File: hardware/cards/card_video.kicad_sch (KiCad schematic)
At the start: 48 parts, among them J1 HDMI_A, J2 VGA HD15, M1 Core2350B (8MB PSRAM), U2 74LVC245A, U3 74LVC245A, U4 74LVC245A, U5 74LVC245A, U6 74LVC245A, U7 74LVC245A

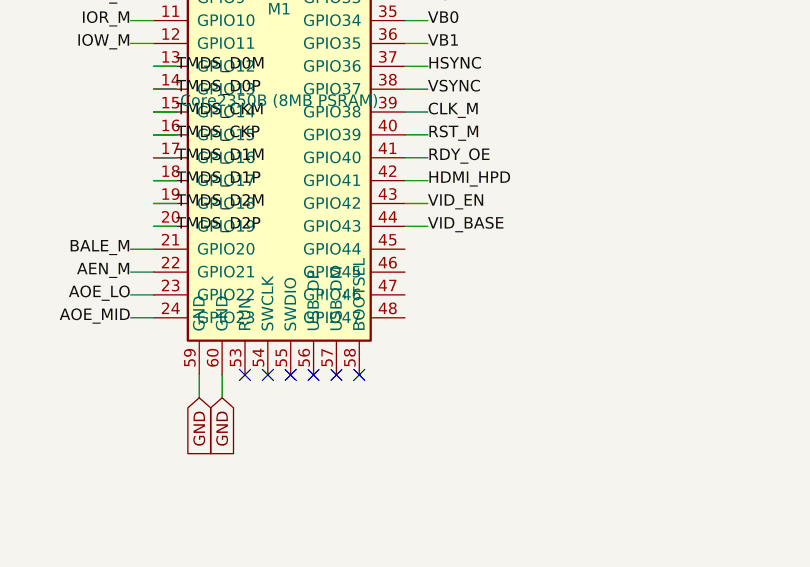
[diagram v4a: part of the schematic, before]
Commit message: ERC cleanup: NC flags on unused pins, anchored interface labels
KiCad 10 ERC drops from 366 to 16 violations, all noise:

- NC flags on the 36 genuinely unused pins (cpu_core '138/'161 spares,
  Supervisor RP2040 unused GPIO, Core2350B GPIO44-47, rtc '138 spares).
- emit_interface anchors every hier label on a stub wire ending in a
  same-name local label -- connectivity unchanged (still by name;
  netlist spans verified), but nothing dangles.
- Interface honesty: cpu_core drops AEN/IOCHRDY from PINS (both live on
  bus_mcu; nothing here touched them), bus_mcu drops PRIV_COUNTER (the
  counter chain is on-sheet, CNT_* never crosses).
- Remaining 6 label_dangling are root IRQ9-13/15: single-sheet by
  design (soft-PIC pull-ups await future 16-bit sources); kept in PINS
  as the AT-style contract.

Co-Authored-By: Claude Fable 5 <noreply@anthropic.com>
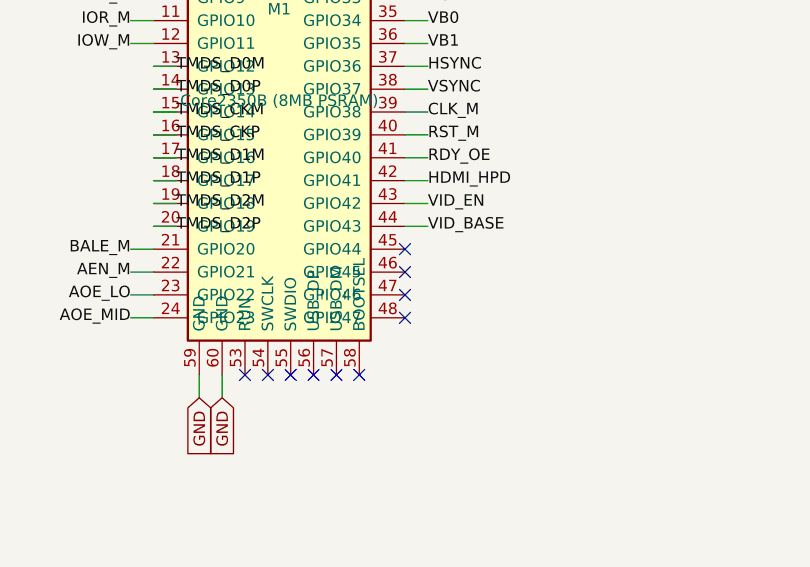
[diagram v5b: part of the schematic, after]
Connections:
- no-connect marks 41 -> 45
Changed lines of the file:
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@@
 		)
+	)
+	(no_connect
+		(at 179.07 161.29)
+	)
+	(no_connect
+		(at 179.07 163.83)
+	)
+	(no_connect
+		(at 179.07 166.37)
+	)
+	(no_connect
+		(at 179.07 168.91)
 	)
 	(wire

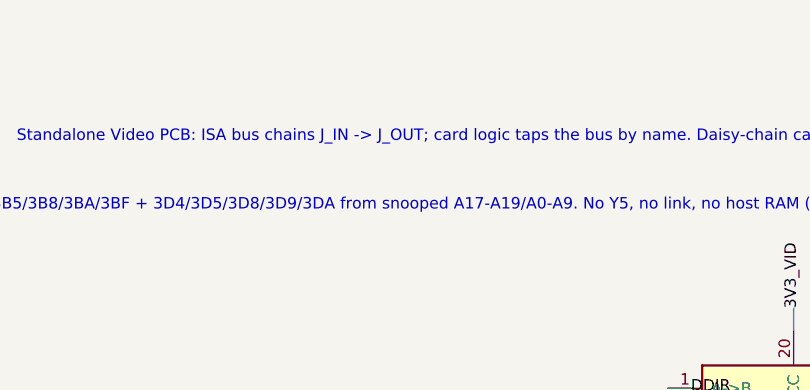
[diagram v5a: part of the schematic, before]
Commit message: ERC power cleanup: single flag owner, flags on series-fed rails
Full-build ERC is now just the 6 expected IRQ9-13/15 label_dangling.

- Root's duplicate PWR_FLAGs removed from build.py: power.py #FLG1-3
  own +5V/+3V3/GND; the pair made flag-vs-flag pin_to_pin errors.
- PWR_FLAGs added on the local rails ERC can't see through a series
  part: VBUS_MCU / VBUS_VID (Schottky diode-OR), VBUS_KBD / HDMI_5V
  (polyfuse), CH224_VDD (1k per WCH ref), AVDD_PGUS / AGND_PGUS
  (ferrite beads).

Net membership verified unchanged: 821 nets, node-identical to HEAD.

Co-Authored-By: Claude Fable 5 <noreply@anthropic.com>
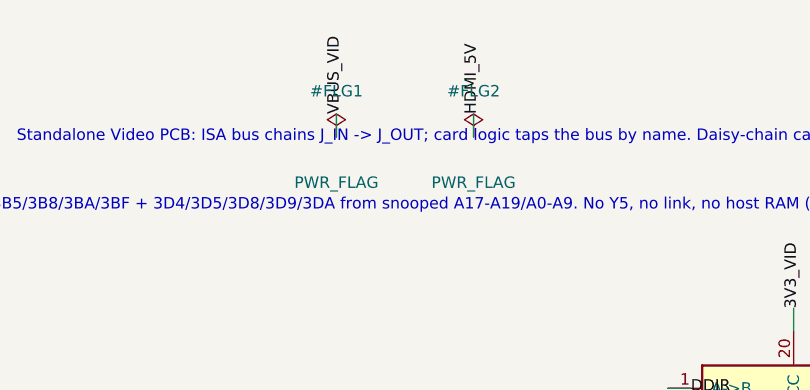
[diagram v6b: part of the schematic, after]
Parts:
- removed F1: 500mA, symbol Device:Polyfuse
- added R10: 270, symbol Device:R
- F1: renamed from R10; value 270 -> 500mA; symbol Device:R -> Device:Polyfuse; LCSC Part Num C22966 -> C46641014
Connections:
- net +5V: now also F1.1
- net HDMI_5V: now also F1.2
- net HDMI_D2P: now also R10.2; no longer F1.2
- net TMDS_D2P: now also R10.1; no longer F1.1
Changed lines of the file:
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@@
 	(wire
 		(pts
+			(xy 12.7 12.7)
+			(xy 12.7 10.16)
+		)
+		(stroke
+			(width 0)
+			(type default)
+		)
+	)
+	(label "VBUS_VID"
+		(at 12.7 10.16 90)
+		(effects
+			(font
+				(size 1.27 1.27)
+			)
+		)
+	)
+	(wire
+		(pts
+			(xy 27.94 12.7)
+			(xy 27.94 10.16)
+		)
+		(stroke
+			(width 0)
+			(type default)
+		)
+	)
+	(label "HDMI_5V"
+		(at 27.94 10.16 90)
+		(effects
+			(font
+				(size 1.27 1.27)
+			)
+		)
+	)
+	(wire
+		(pts
 			(xy 44.45 270.51)
 			(xy 44.45 267.97)
@@
 					(unit 1)
 				)
+			)
+		)
+	)
+	(symbol
+		(lib_id "power:PWR_FLAG")
+		(at 12.7 12.7 0)
+		(unit 1)
+		(exclude_from_sim no)
+		(in_bom yes)
+		(on_board yes)
+		(dnp no)
+		(fields_autoplaced yes)
+		(property "Reference" "#FLG1"
+			(at 12.7 7.62 0)
+			(effects
+				(font
+					(size 1.27 1.27)
+				)
+			)
+		)
+		(property "Value" "PWR_FLAG"
+			(at 12.7 17.78 0)
+			(effects
+				(font
+					(size 1.27 1.27)
+				)
+			)
+		)
+		(property "Footprint" ""
+			(at 12.7 12.7 0)
+			(effects
+				(font
+					(size 1.27 1.27)
+				)
+				(hide yes)
+			)
+		)
+		(pin "1"
+		)
+		(instances
+			(project "card_video"
+				(path "/6b5ebf7b-92ce-58a1-8c1d-03e449d8e3c9"
+					(reference "#FLG1")
+					(unit 1)
+				)
+			)
+		)
+	)
+	(symbol
+		(lib_id "power:PWR_FLAG")
+		(at 27.94 12.7 0)
+		(unit 1)
+		(exclude_from_sim no)
+		(in_bom yes)
+		(on_board yes)
+		(dnp no)
+		(fields_autoplaced yes)
+		(property "Reference" "#FLG2"
+			(at 27.94 7.62 0)
+			(effects
+				(font
+					(size 1.27 1.27)
+				)
+			)
+		)
+		(property "Value" "PWR_FLAG"
+			(at 27.94 17.78 0)
+			(effects
+				(font
+					(size 1.27 1.27)
+				)
+			)
+		)
+		(property "Footprint" ""
+			(at 27.94 12.7 0)
+			(effects
+				(font
+					(size 1.27 1.27)
+				)
+				(hide yes)
+			)
+		)
+		(pin "1"
+		)
+		(instances
+			(project "card_video"
+				(path "/6b5ebf7b-92ce-58a1-8c1d-03e449d8e3c9"
+					(reference "#FLG2")
+					(unit 1)
+				)

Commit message: Parts: footprints for all components, close 6 LCSC map gaps, check_parts.py
- mxsch.py emits the Footprint property from component props (was
  hard-coded empty); parts.py entries now carry a verified KiCad
  footprint, applied at build time alongside the LCSC number.
- Map keys fixed to match placed values: USB_PROG, SS34, LED (PicoGUS),
  APS6404L, CB3T3257/45 -- every combo across all sheets + cards now
  resolves (130 combos, 455 netlist components, all with footprints).
- Package corrections from JLC DB re-check: RTL8019AS is QFP-100 14x20
  P0.65 (not TQFP); C2897411 female header is a 2x10 strip -- fine for
  Core2350B, Pico needs 2x 1x20 (noted in jlcpcb-sourcing.md).
- 10 mini-xt:* placeholder footprints mark parts whose land pattern is
  authored at layout from the EasyEDA data (CH224K, magnetics, RJ45,
  HDMI, CF socket, ISA slot, switches, Core2350B PGA).
- New tools/check_parts.py: fails on unmapped combos, missing fp
  fields, or footprints absent from the installed KiCad libs.

Co-Authored-By: Claude Fable 5 <noreply@anthropic.com>
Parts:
- C1, C2, C4, C5, C6, C7: footprint (none) -> Capacitor_SMD:C_0603_1608Metric
- C3: footprint (none) -> Capacitor_SMD:C_0805_2012Metric
- D1: footprint (none) -> Diode_SMD:D_SMA; LCSC Part Num (none) -> C8678
- F1: footprint (none) -> Fuse:Fuse_1206_3216Metric
- J1: footprint (none) -> mini-xt:HDMI_A_SHOUHAN_043
- J2: footprint (none) -> Connector_Dsub:DSUB-15-HD_Socket_Horizontal_P2.29x2.54mm_EdgePinOffset8.35mm_Housed_MountingHolesOffset10.89mm
- JP1, JP2: footprint (none) -> Connector_PinHeader_2.54mm:PinHeader_1x02_P2.54mm_Vertical
- J_IN, J_OUT: footprint (none) -> Connector_PinHeader_2.54mm:PinHeader_2x30_P2.54mm_Vertical
- M1: footprint (none) -> mini-xt:Core2350B_PGA
- R10, R11, R12, R13, R14, R15, R16, R17, R20, R21, R22, R23, R24, R25, R26, R27, R28, R29, R30, R31, R32, R33, R34, R35, R36, R37: footprint (none) -> Resistor_SMD:R_0603_1608Metric
- U2, U3, U4, U5, U6, U7: footprint (none) -> Package_SO:TSSOP-20_4.4x6.5mm_P0.65mm
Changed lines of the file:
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@@
 			)
 		)
-		(property "Footprint" ""
+		(property "Footprint" "Connector_PinHeader_2.54mm:PinHeader_2x30_P2.54mm_Vertical"
 			(at 444.5 152.4 0)
 			(effects
@@
 			)
 		)
-		(property "Footprint" ""
+		(property "Footprint" "Connector_PinHeader_2.54mm:PinHeader_2x30_P2.54mm_Vertical"
 			(at 508 152.4 0)
 			(effects
@@
 			)
 		)
-		(property "Footprint" ""
+		(property "Footprint" "mini-xt:Core2350B_PGA"
 			(at 165.1 139.7 0)
 			(effects
@@
 			)
 		)
-		(property "Footprint" ""
+		(property "Footprint" "Diode_SMD:D_SMA"
+			(at 152.4 40.64 0)
+			(effects
+				(font
+					(size 1.27 1.27)
+				)
+				(hide yes)
+			)
+		)
+		(property "LCSC Part Num" "C8678"
 			(at 152.4 40.64 0)
 			(effects
@@
 			)
 		)
-		(property "Footprint" ""
+		(property "Footprint" "Capacitor_SMD:C_0603_1608Metric"
 			(at 44.45 274.32 0)
 			(effects
@@
 			)
 		)
-		(property "Footprint" ""
+		(property "Footprint" "Capacitor_SMD:C_0603_1608Metric"
 			(at 69.85 274.32 0)
 			(effects
@@
 			)
 		)
-		(property "Footprint" ""
+		(property "Footprint" "Capacitor_SMD:C_0805_2012Metric"
 			(at 95.25 274.32 0)
 			(effects
@@
 			)
 		)
-		(property "Footprint" ""
+		(property "Footprint" "Capacitor_SMD:C_0603_1608Metric"
 			(at 127 274.32 0)
 			(effects
@@
 			)
 		)
-		(property "Footprint" ""
+		(property "Footprint" "Capacitor_SMD:C_0603_1608Metric"
 			(at 152.4 274.32 0)
 			(effects
@@
 			)
 		)
-		(property "Footprint" ""
+		(property "Footprint" "Capacitor_SMD:C_0603_1608Metric"
 			(at 177.8 274.32 0)
 			(effects
@@
 			)
 		)
-		(property "Footprint" ""
+		(property "Footprint" "Capacitor_SMD:C_0603_1608Metric"
 			(at 203.2 274.32 0)
 			(effects
@@
 			)
 		)
-		(property "Footprint" ""
+		(property "Footprint" "Resistor_SMD:R_0603_1608Metric"
 			(at 33.02 287.02 0)
 			(effects
@@
 			)
 		)
-		(property "Footprint" ""
+		(property "Footprint" "Resistor_SMD:R_0603_1608Metric"
 			(at 48.26 287.02 0)
 			(effects
@@
 			)
 		)
-		(property "Footprint" ""
+		(property "Footprint" "Resistor_SMD:R_0603_1608Metric"
 			(at 63.5 287.02 0)
 			(effects
@@
 			)
 		)
-		(property "Footprint" ""
+		(property "Footprint" "Resistor_SMD:R_0603_1608Metric"
 			(at 78.74 287.02 0)
 			(effects
@@
 			)
 		)
-		(property "Footprint" ""
+		(property "Footprint" "Resistor_SMD:R_0603_1608Metric"
 			(at 93.98 287.02 0)
 			(effects
@@
 			)
 		)
-		(property "Footprint" ""
+		(property "Footprint" "Resistor_SMD:R_0603_1608Metric"
 			(at 109.22 287.02 0)
 			(effects
@@
 			)
 		)
-		(property "Footprint" ""
+		(property "Footprint" "Connector_PinHeader_2.54mm:PinHeader_1x02_P2.54mm_Vertical"
 			(at 121.92 40.64 0)
 			(effects
@@
 			)
 		)
-		(property "Footprint" ""
+		(property "Footprint" "Connector_PinHeader_2.54mm:PinHeader_1x02_P2.54mm_Vertical"
 			(at 137.16 40.64 0)
 			(effects
@@
 			)
 		)
-		(property "Footprint" ""
+		(property "Footprint" "Resistor_SMD:R_0603_1608Metric"
 			(at 121.92 60.96 0)
 			(effects
@@
 			)
 		)
-		(property "Footprint" ""
+		(property "Footprint" "Resistor_SMD:R_0603_1608Metric"
 			(at 137.16 60.96 0)
 			(effects
@@
 			)
 		)
-		(property "Footprint" ""
+		(property "Footprint" "Package_SO:TSSOP-20_4.4x6.5mm_P0.65mm"
 			(at 63.5 50.8 0)
 			(effects
@@
 			)
 		)
-		(property "Footprint" ""
+		(property "Footprint" "Package_SO:TSSOP-20_4.4x6.5mm_P0.65mm"
 			(at 63.5 99.06 0)
 			(effects
@@
 			)
 		)
-		(property "Footprint" ""
+		(property "Footprint" "Package_SO:TSSOP-20_4.4x6.5mm_P0.65mm"
 			(at 63.5 147.32 0)
 			(effects
@@
 			)
 		)
-		(property "Footprint" ""
+		(property "Footprint" "Package_SO:TSSOP-20_4.4x6.5mm_P0.65mm"
 			(at 63.5 195.58 0)
 			(effects
@@
 			)
 		)
-		(property "Footprint" ""
+		(property "Footprint" "Package_SO:TSSOP-20_4.4x6.5mm_P0.65mm"
 			(at 63.5 243.84 0)
 			(effects
@@
 			)
 		)
-		(property "Footprint" ""
+		(property "Footprint" "Package_SO:TSSOP-20_4.4x6.5mm_P0.65mm"
 			(at 109.22 243.84 0)
 			(effects
@@
 			)
 		)
-		(property "Footprint" ""
+		(property "Footprint" "Fuse:Fuse_1206_3216Metric"
 			(at 297.18 170.18 0)
 			(effects
@@
 			)
 		)
-		(property "Footprint" ""
+		(property "Footprint" "mini-xt:HDMI_A_SHOUHAN_043"
 			(at 322.58 88.9 0)
 			(effects
@@
 			)
 		)
-		(property "Footprint" ""
+		(property "Footprint" "Resistor_SMD:R_0603_1608Metric"
 			(at 289.56 45.72 0)
 			(effects
@@
 			)
 		)
-		(property "Footprint" ""
+		(property "Footprint" "Resistor_SMD:R_0603_1608Metric"
 			(at 289.56 60.96 0)
 			(effects
@@
 			)
 		)
-		(property "Footprint" ""
+		(property "Footprint" "Resistor_SMD:R_0603_1608Metric"
 			(at 289.56 76.2 0)
 			(effects
@@
 			)
 		)
-		(property "Footprint" ""
+		(property "Footprint" "Resistor_SMD:R_0603_1608Metric"
 			(at 289.56 91.44 0)
 			(effects
@@
 			)
 		)
-		(property "Footprint" ""
+		(property "Footprint" "Resistor_SMD:R_0603_1608Metric"
 			(at 289.56 106.68 0)
 			(effects
@@
 			)
 		)
-		(property "Footprint" ""
+		(property "Footprint" "Resistor_SMD:R_0603_1608Metric"
 			(at 289.56 121.92 0)
 			(effects
@@
 			)
 		)
-		(property "Footprint" ""
+		(property "Footprint" "Resistor_SMD:R_0603_1608Metric"
 			(at 289.56 137.16 0)
 			(effects
@@
 			)
 		)
-		(property "Footprint" ""
+		(property "Footprint" "Resistor_SMD:R_0603_1608Metric"
 			(at 289.56 152.4 0)
 			(effects
@@
 			)
 		)
-		(property "Footprint" ""
+		(property "Footprint" "Resistor_SMD:R_0603_1608Metric"
 			(at 266.7 165.1 0)
 			(effects
@@
 			)
 		)
-		(property "Footprint" ""
+		(property "Footprint" "Resistor_SMD:R_0603_1608Metric"
 			(at 266.7 180.34 0)
 			(effects
@@
 			)
 		)
-		(property "Footprint" ""
+		(property "Footprint" "Resistor_SMD:R_0603_1608Metric"
 			(at 266.7 195.58 0)
 			(effects
@@
 			)
 		)
-		(property "Footprint" ""
+		(property "Footprint" "Resistor_SMD:R_0603_1608Metric"
 			(at 266.7 210.82 0)
 			(effects
@@
 			)
 		)
-		(property "Footprint" ""
+		(property "Footprint" "Resistor_SMD:R_0603_1608Metric"
 			(at 266.7 226.06 0)
 			(effects
@@
 			)
 		)
-		(property "Footprint" ""
+		(property "Footprint" "Resistor_SMD:R_0603_1608Metric"
 			(at 266.7 241.3 0)
 			(effects
@@
 			)
 		)
-		(property "Footprint" ""
+		(property "Footprint" "Resistor_SMD:R_0603_1608Metric"
 			(at 266.7 256.54 0)
 			(effects
@@
 			)
 		)
-		(property "Footprint" ""
+		(property "Footprint" "Resistor_SMD:R_0603_1608Metric"
 			(at 266.7 271.78 0)
 			(effects
@@
 			)
 		)
-		(property "Footprint" ""
+		(property "Footprint" "Resistor_SMD:R_0603_1608Metric"
 			(at 266.7 287.02 0)
 			(effects
@@
 			)
 		)
-		(property "Footprint" ""
+		(property "Footprint" "Resistor_SMD:R_0603_1608Metric"
 			(at 281.94 287.02 0)
 			(effects
@@
 			)
 		)
-		(property "Footprint" ""
+		(property "Footprint" "Connector_Dsub:DSUB-15-HD_Socket_Horizontal_P2.29x2.54mm_EdgePinOffset8.35mm_Housed_MountingHolesOffset10.89mm"
 			(at 322.58 215.9 0)
 			(effects
